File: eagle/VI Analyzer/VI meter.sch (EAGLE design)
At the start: 63 parts, among them IC2 E50D, IC3 LM358D, J4 MF-CON-MICROUSB-RIGHT, SW2 Load Switch, SW3 Hi Res, SW4 Hi Res

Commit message: ADD: Hi res current reading from ads1115
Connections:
- net I-OUT renamed ACS-OUT
- net N$36 renamed POT_OFFSET
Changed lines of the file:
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@@
 </segment>
 </net>
-<net name="I-OUT" class="0">
+<net name="ACS-OUT" class="0">
 <segment>
 <pinref part="U$5" gate="G$1" pin="IP-@3"/>
@@
 </segment>
 </net>
-<net name="N$36" class="0">
+<net name="POT_OFFSET" class="0">
 <segment>
 <pinref part="R24" gate="G$1" pin="2"/>

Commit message: Fix: moved the shunt to the lower side, single channel amp instead of differential
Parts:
- removed R7: 1K, rcl:R-US_M1206
- removed R8: 330K, rcl:R-US_M1206
- removed U$8: PH-JST-2-ANGLE, dragCustom:PH-JST-2-ANGLE
- added OSCILLOSCOPE, X1, X3: 22-23-2021, con-molex:22-23-2021
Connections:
- removed net ACS-OUT: R4.1, R7.2, SW3.1F, U$5.IP-@3, U$5.IP-@4
- removed net GND2: C3.2, C4.2, U$5.GND
- removed net N$5: IC3B.+IN, R7.1, R8.1
- removed net OUT+\: R4.2, R6.2, SW2.1F, SW3.1
- removed net VCC2: C3.1, U$5.VCC
- new net LOAD-: IC3B.+IN, R4.1, SW3.1F, U$3.P$1, X2.4
- new net N$6: SW2.1F, U$5.IP-@3, U$5.IP-@4
- net AMPED_ACS_OUT: now also X3-2.S
- net GND: now also C3.2, C4.2, OSCILLOSCOPE-1.S, R4.2, R6.2, SW3.1, U$5.GND, X1-1.S, X3-1.S; no longer R8.2, U$3.P$1, U$8.P$1, X2.4
- net HI_RES_CURRENT: now also OSCILLOSCOPE-2.S
- net IN+: now also X1-2.S; no longer U$8.P$2
- net VCC: now also C3.1, U$5.VCC
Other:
- note added: "Oscilloscope Tap"
- moved on the sheet: C10, C25, C5, C9, D7, IC3A, IC3B, R11, R12, R13, R16, R22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

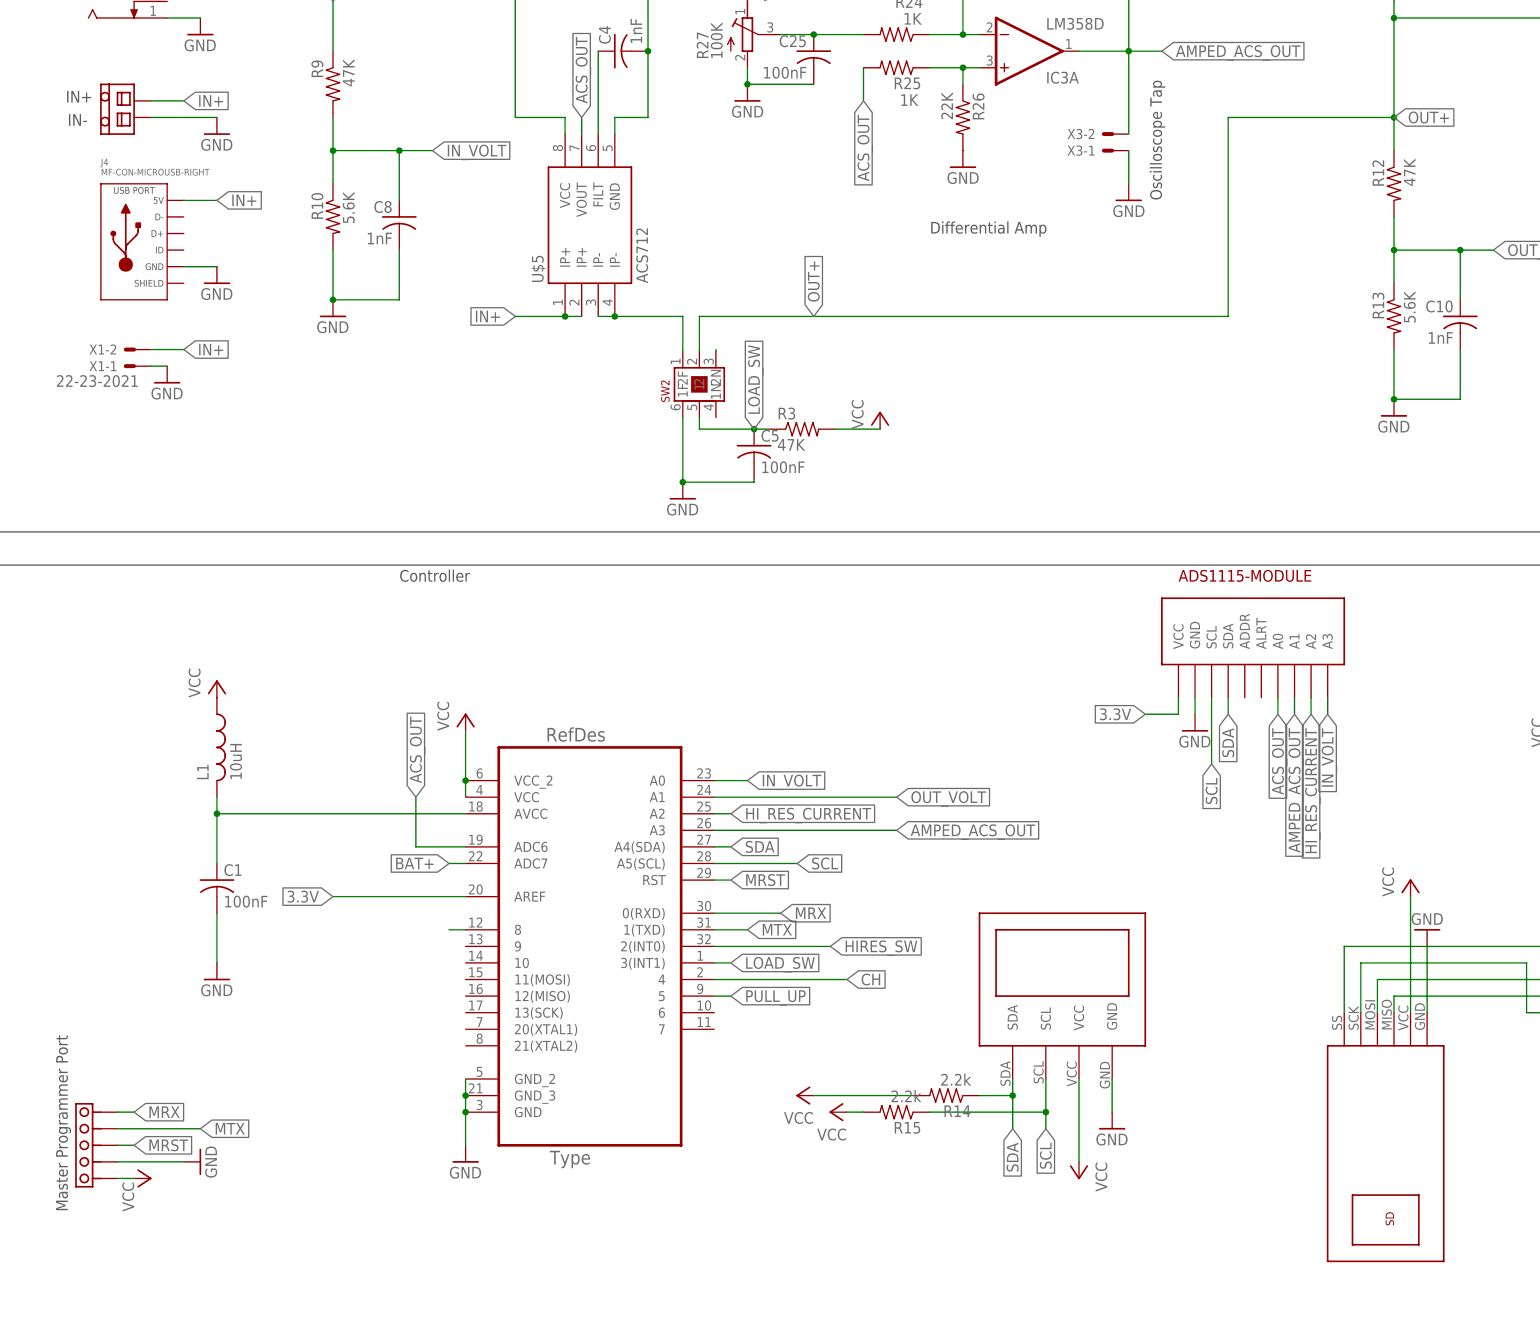
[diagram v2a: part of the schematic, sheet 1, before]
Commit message: Edit: fixed source voltage, can be improved with more granular peice-wise equations
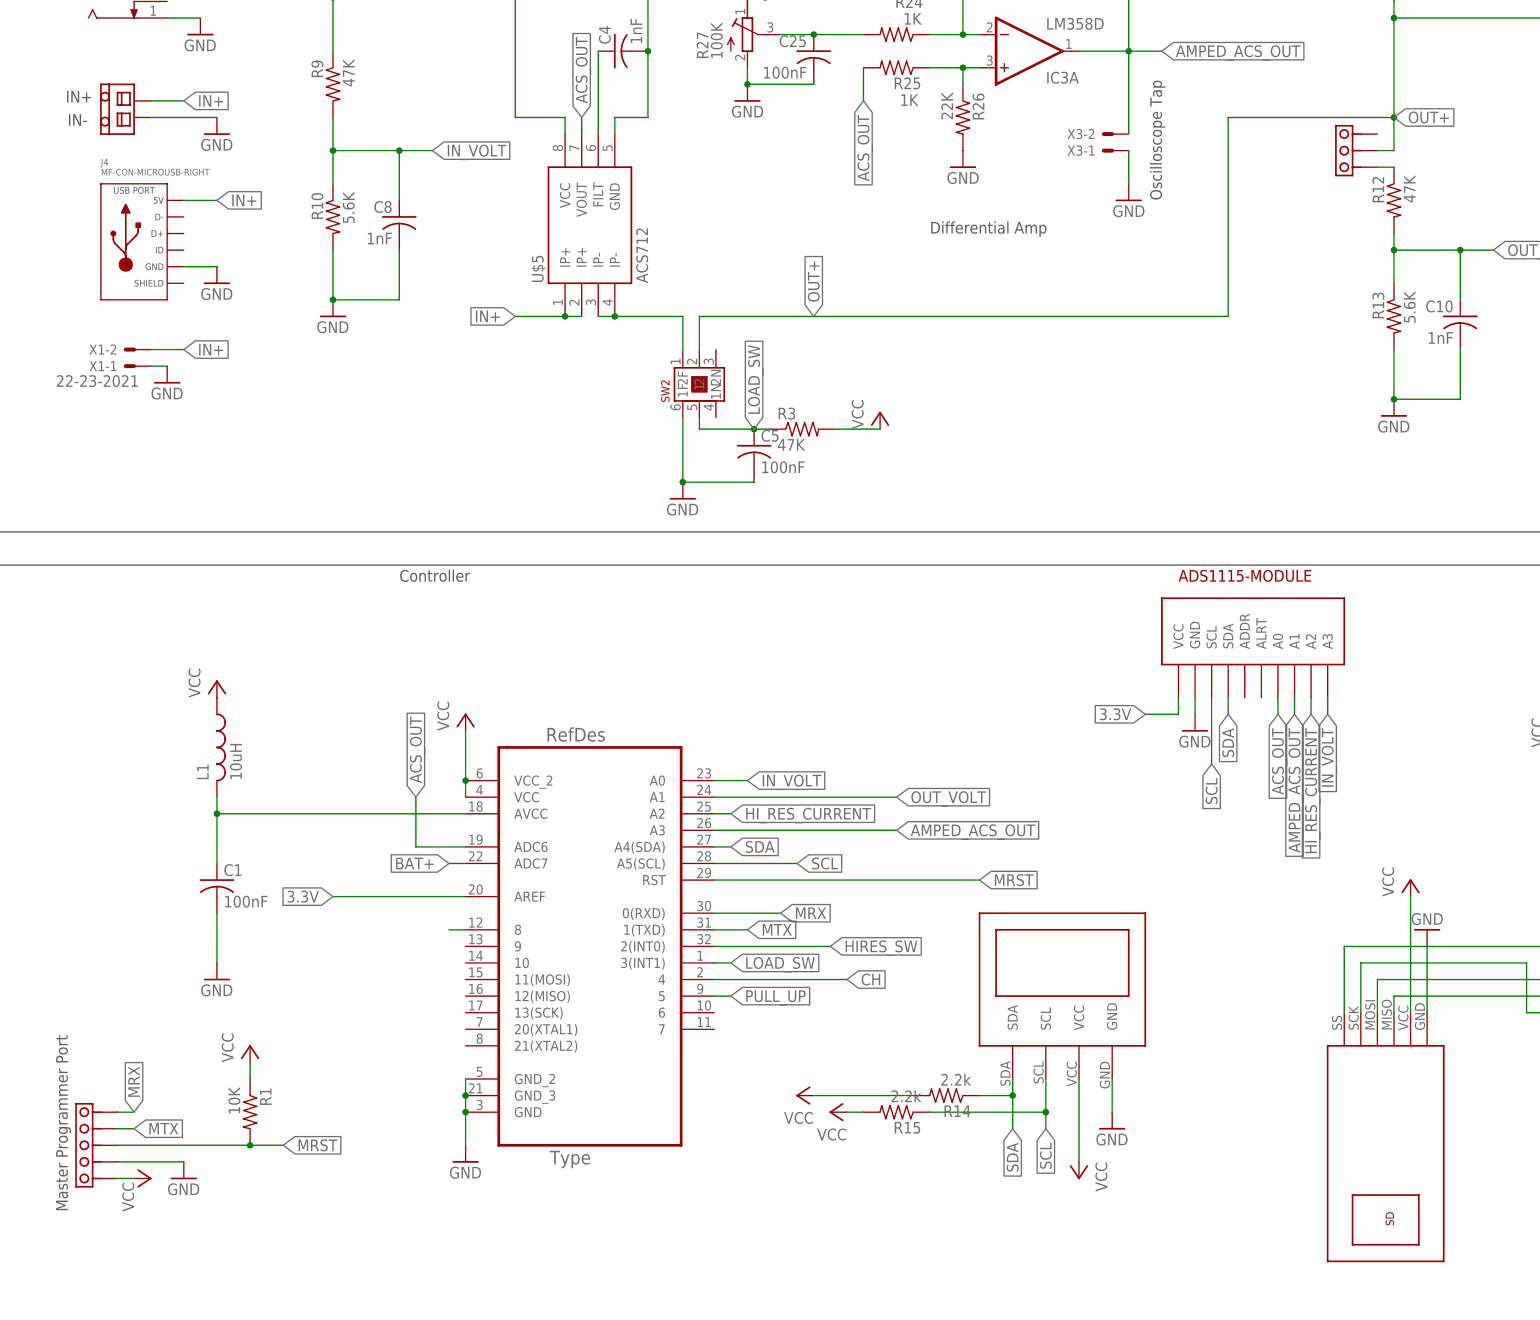
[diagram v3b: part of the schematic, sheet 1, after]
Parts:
- added R1: 10K, rcl:R-US_M1206
- added U$8: BERG_3, dragCustom:BERG_3
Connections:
- new net N$5: R12.1, U$8.P$3
- net MRST: now also R1.2
- net OUT+: now also U$8.P$2; no longer R12.1
- net VCC: now also R1.1
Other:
- moved on the sheet: R12
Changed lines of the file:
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@@
 <part name="OSCILLOSCOPE" library="con-molex" library_urn="urn:adsk.eagle:library:165" deviceset="22-23-2021" device=""/>
 <part name="GND25" library="supply1" library_urn="urn:adsk.eagle:library:371" deviceset="GND" device=""/>
+<part name="U$8" library="dragCustom" deviceset="BERG_3" device=""/>
+<part name="R1" library="rcl" library_urn="urn:adsk.eagle:library:334" deviceset="R-US_" device="M1206" package3d_urn="urn:adsk.eagle:package:23566/1" value="10K"/>
+<part name="P+16" library="supply1" deviceset="VCC" device=""/>
 </parts>
 <sheets>
@@
 <attribute name="VALUE" x="30.48" y="-154.94" size="1.778" layer="96" rot="R90"/>
 </instance>
-<instance part="GND13" gate="1" x="40.64" y="-147.32" rot="R90"/>
+<instance part="GND13" gate="1" x="38.1" y="-149.86"/>
 <instance part="X2" gate="G$1" x="274.32" y="53.34" rot="R90"/>
 <instance part="C1" gate="G$1" x="43.18" y="-104.14"/>
@@
 <instance part="P+5" gate="VCC" x="312.674" y="-17.78"/>
 <instance part="C9" gate="G$1" x="312.674" y="-35.052"/>
-<instance part="R12" gate="G$1" x="223.52" y="2.54" rot="MR270"/>
+<instance part="R12" gate="G$1" x="223.52" y="0" rot="MR270"/>
 <instance part="R13" gate="G$1" x="223.52" y="-17.78" rot="MR270"/>
 <instance part="GND16" gate="1" x="223.52" y="-33.02"/>
@@
 <instance part="OSCILLOSCOPE" gate="-2" x="350.52" y="2.54" rot="R180"/>
 <instance part="GND25" gate="1" x="353.06" y="-10.16"/>
+<instance part="U$8" gate="G$1" x="215.9" y="7.62"/>
+<instance part="R1" gate="G$1" x="48.26" y="-139.7" rot="R270"/>
+<instance part="P+16" gate="VCC" x="48.26" y="-129.54"/>
 </instances>
 <busses>
@@
 <junction x="88.9" y="35.56"/>
 </segment>
+<segment>
+<pinref part="R1" gate="G$1" pin="1"/>
+<pinref part="P+16" gate="VCC" pin="VCC"/>
+<wire x1="48.26" y1="-132.08" x2="48.26" y2="-134.62" width="0.1524" layer="91"/>
+</segment>
 </net>
 <net name="N$2" class="0">
@@
 <wire x1="198.12" y1="-17.78" x2="198.12" y2="12.7" width="0.1524" layer="91"/>
 <label x="223.52" y="12.7" size="1.778" layer="95" xref="yes"/>
-<pinref part="R12" gate="G$1" pin="1"/>
 <wire x1="223.52" y1="30.48" x2="223.52" y2="27.94" width="0.1524" layer="91"/>
 <pinref part="D7" gate="G$1" pin="C"/>
 <wire x1="223.52" y1="27.94" x2="223.52" y2="12.7" width="0.1524" layer="91"/>
-<wire x1="223.52" y1="12.7" x2="223.52" y2="7.62" width="0.1524" layer="91"/>
 <wire x1="198.12" y1="12.7" x2="223.52" y2="12.7" width="0.1524" layer="91"/>
-<junction x="223.52" y="12.7"/>
 <pinref part="U$3" gate="G$1" pin="P$2"/>
 <wire x1="271.78" y1="27.94" x2="256.54" y2="27.94" width="0.1524" layer="91"/>
@@
 <wire x1="256.54" y1="50.8" x2="256.54" y2="27.94" width="0.1524" layer="91"/>
 <junction x="256.54" y="27.94"/>
+<pinref part="U$8" gate="G$1" pin="P$2"/>
+<wire x1="220.98" y1="7.62" x2="223.52" y2="7.62" width="0.1524" layer="91"/>
+<wire x1="223.52" y1="7.62" x2="223.52" y2="12.7" width="0.1524" layer="91"/>
+<junction x="223.52" y="12.7"/>
 </segment>
 </net>
@@
 <pinref part="R12" gate="G$1" pin="2"/>
 <pinref part="R13" gate="G$1" pin="1"/>
-<wire x1="223.52" y1="-2.54" x2="223.52" y2="-7.62" width="0.1524" layer="91"/>
+<wire x1="223.52" y1="-5.08" x2="223.52" y2="-7.62" width="0.1524" layer="91"/>
 <wire x1="223.52" y1="-7.62" x2="223.52" y2="-12.7" width="0.1524" layer="91"/>
 <wire x1="223.52" y1="-7.62" x2="233.68" y2="-7.62" width="0.1524" layer="91"/>
@@
 <pinref part="U$4" gate="G$1" pin="P$1"/>
 <wire x1="27.94" y1="-139.7" x2="30.48" y2="-139.7" width="0.1524" layer="91"/>
-<label x="30.48" y="-139.7" size="1.778" layer="95" xref="yes"/>
+<label x="30.48" y="-139.7" size="1.778" layer="95" rot="R90" xref="yes"/>
 </segment>
 <segment>
@@
 <segment>
 <pinref part="U$4" gate="G$1" pin="P$2"/>
-<wire x1="27.94" y1="-142.24" x2="40.64" y2="-142.24" width="0.1524" layer="91"/>
-<label x="40.64" y="-142.24" size="1.778" layer="95" xref="yes"/>
+<wire x1="27.94" y1="-142.24" x2="30.48" y2="-142.24" width="0.1524" layer="91"/>
+<label x="30.48" y="-142.24" size="1.778" layer="95" xref="yes"/>
 </segment>
 <segment>
@@
 <segment>
 <pinref part="U$2" gate="G$1" pin="RST"/>
-<wire x1="119.38" y1="-104.14" x2="121.92" y2="-104.14" width="0.1524" layer="91"/>
-<label x="121.92" y="-104.14" size="1.778" layer="95" xref="yes"/>
-</segment>
-<segment>
+<wire x1="119.38" y1="-104.14" x2="160.02" y2="-104.14" width="0.1524" layer="91"/>
+<label x="160.02" y="-104.14" size="1.778" layer="95" xref="yes"/>
+</segment>
+<segment>
+<label x="53.34" y="-144.78" size="1.778" layer="95" xref="yes"/>
 <pinref part="U$4" gate="G$1" pin="P$3"/>
-<wire x1="27.94" y1="-144.78" x2="30.48" y2="-144.78" width="0.1524" layer="91"/>
-<label x="30.48" y="-144.78" size="1.778" layer="95" xref="yes"/>
+<wire x1="53.34" y1="-144.78" x2="48.26" y2="-144.78" width="0.1524" layer="91"/>
+<pinref part="R1" gate="G$1" pin="2"/>
+<wire x1="48.26" y1="-144.78" x2="27.94" y2="-144.78" width="0.1524" layer="91"/>
+<junction x="48.26" y="-144.78"/>
 </segment>
 </net>
@@
 </segment>
 </net>
+<net name="N$5" class="0">
+<segment>
+<pinref part="U$8" gate="G$1" pin="P$3"/>
+<pinref part="R12" gate="G$1" pin="1"/>
+<wire x1="220.98" y1="5.08" x2="223.52" y2="5.08" width="0.1524" layer="91"/>
+</segment>
+</net>
